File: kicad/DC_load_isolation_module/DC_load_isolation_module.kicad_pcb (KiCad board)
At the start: 2 copper layers, 110 x 60 mm, 200 parts, among them J1 Iso board connector, J12 Iso board connector, J2 USB_C_Receptacle_USB2.0_16P, Q1 MMBT5551L, Q10 AO3400A, Q11 AO3400A, Q12 MMBT5551L, Q13 AO3400A, Q14 MMBT5401, Q15 MMBT5551L, Q16 MMBT5551L, Q17 MMBT5401, Q18 MMBT5401, Q2 MMBT5401, Q26 MMBT5551L, Q27 MMBT5551L, Q28 MMBT5551L, Q29 MMBT5551L, Q3 MMBT5401, Q4 MMBT5551L, Q5 MMBT5401, Q6 MMBT5551L, Q7 MMBT5551L, Q8 MMBT5551L, Q9 MMBT5401, T1 UMEC_UT20A13S, T2 UMEC_UT20A13S, U1 LTV-817S, U2 MC34063AD, U3 LTV-817S, U4 CH340C, U5 74HC14D653

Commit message: Routing.
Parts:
- moved C53 4.29 mm to (136.2, 159.6), turned to 90 degrees
- moved C47 3.33 mm to (140.7, 159.6), turned to 90 degrees
- moved C49 1.41 mm to (139.2, 159.6), turned to 90 degrees
- moved R42 1.03 mm to (142.3, 159.6), turned to 90 degrees
- moved C51 0.78 mm to (137.7, 159.6), turned to 90 degrees
- moved D24 0.40 mm to (143.8, 184.3)
- moved R19 0.30 mm to (119.2, 156.3)
- moved Q12 0.28 mm to (116.4, 156.3)
- moved R49 0.14 mm to (130.5, 166.5)
- moved R40 0.10 mm to (134.2, 166.5)
- moved Q26 0.08 mm to (145.7, 171.9)
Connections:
- U5 pad 11: GND -> Earth
- U5 pad 13: GND -> Earth
- U5 pad 5: GND -> Earth
- U5 pad 9: GND -> Earth
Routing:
- net Earth: track 20.9 -> 71.0 mm, vias 19 -> 61
- net Net-(D19-K): track 0.00 -> 36.7 mm, vias 0 -> 1
- net 5V: track 53.1 -> 87.2 mm, vias 9 -> 14
- net Net-(JP1-B): track 0.00 -> 33.6 mm
- net 12V: track 0.00 -> 31.0 mm, vias 1 -> 8
- net Net-(Q26-C): track 0.00 -> 24.1 mm, vias 0 -> 1
- net GND: track 7.68 -> 30.9 mm, vias 8 -> 24
- net Net-(Q10-D): track 0.00 -> 19.8 mm
- net Net-(D4-K): track 0.00 -> 17.8 mm, vias 0 -> 1
- net ~{TF_GATE}: track 0.00 -> 17.5 mm, vias 0 -> 1
- net Net-(JP5-A): track 0.00 -> 16.1 mm, vias 1 -> 2
- net Net-(Q26-E): track 0.00 -> 15.0 mm, vias 0 -> 1
- net 11V: track 0.00 -> 14.5 mm, vias 0 -> 1
- net Net-(D3-K): track 0.00 -> 12.5 mm, vias 0 -> 2
- net 11V_SRF: track 0.00 -> 12.3 mm, vias 0 -> 1
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
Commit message: Connectors fixed.
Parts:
- added J3: Conn_01x03_Pin, Connector_PinHeader_2.54mm:PinHeader_1x03_P2.54mm_Vertical, F.Cu at (126.1, 189.8)
- J1: value Iso board connector -> PC referenced connector
- J12: value Iso board connector -> Load referenced connector; moved to F.Cu
- TP2, TP3: moved to F.Cu
- moved J1 102.8 mm to (157.7, 152.7)
- moved J12 45.1 mm to (52.3, 152.7), turned to 0 degrees
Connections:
- net 11V renamed /Isolated supply/11V
- net 11V_SRF renamed /Self resonating flyback/11V_SRF
- net 12V renamed 12V_PC
- net 5V renamed 5V_PC
- J1 pad 2: unconnected-(J1-Pin_2-Pad2) -> Earth
- J1 pad 3: unconnected-(J1-Pin_3-Pad3) -> 5V_PC_PC
- J1 pad 4: unconnected-(J1-Pin_4-Pad4) -> Earth
- J1 pad 8: GND -> unconnected-(J1-Pin_8-Pad8)
- J12 pad 2: 3V3 -> GND
- J12 pad 4: TX_3V3 -> GND
- J12 pad 5: GND -> TX_3V3
- J12 pad 6: 12V_EXT -> GND
- J12 pad 7: 5V_EXT -> 3V3
- J12 pad 8: Earth -> GND

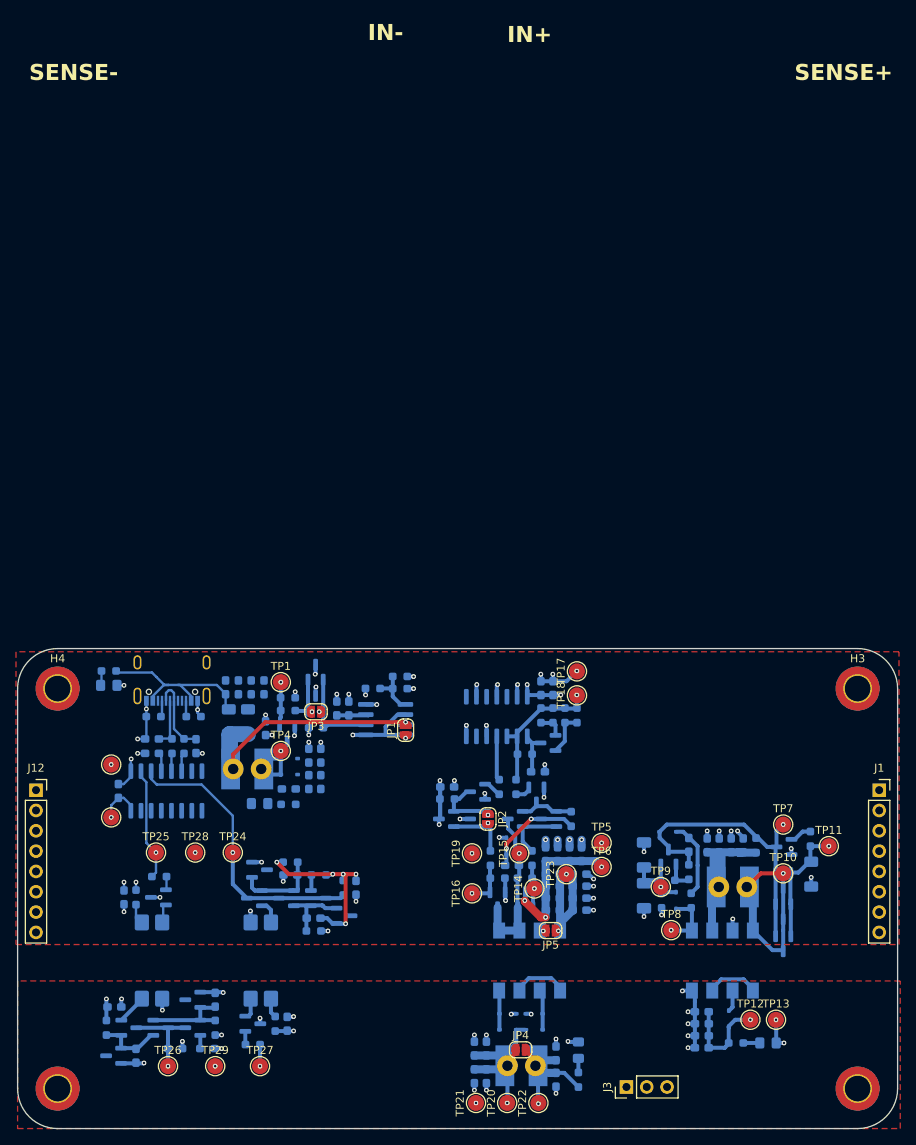
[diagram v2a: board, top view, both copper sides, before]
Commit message: Iso module almost done.
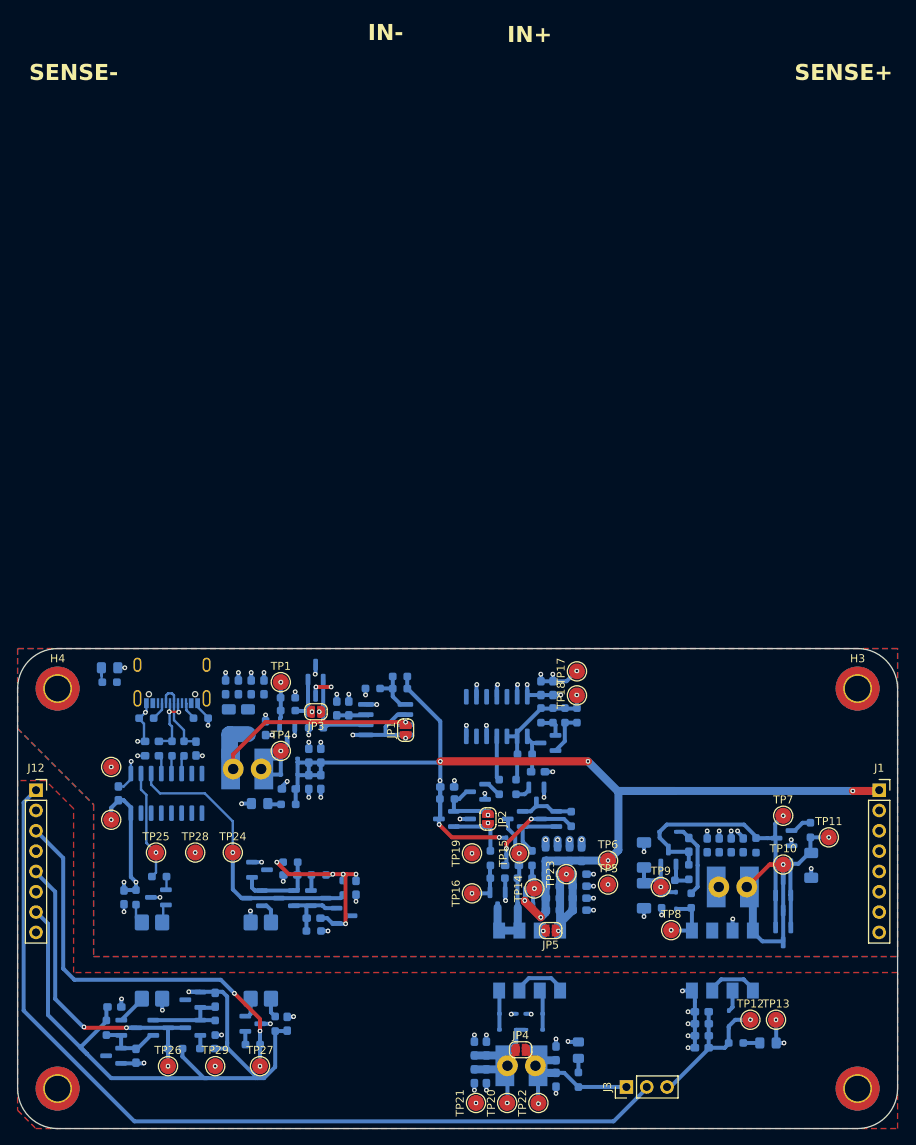
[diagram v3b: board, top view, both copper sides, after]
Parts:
- H1, H2: moved to F.Cu
- moved TP5 5.26 mm to (123.8, 164.5)
- moved D10 2.20 mm to (61.5, 137.4)
- moved R32 1.40 mm to (61.5, 139.2)
- moved TP6 1.13 mm to (123.8, 161.5)
- moved Q29 1.10 mm to (145.8, 158.7)
- moved Q26 1.10 mm to (145.7, 170.8)
- moved Q27 1.10 mm to (145.7, 166.8)
- moved Q28 1.10 mm to (145.7, 162.9)
- moved R47 1.10 mm to (149.2, 162.1)
- moved R48 1.10 mm to (149.1, 157.7)
- moved TP10 1.10 mm to (145.7, 162.0)
- moved TP11 1.10 mm to (151.4, 158.6)
- moved TP7 1.10 mm to (145.7, 155.9)
- moved R34 0.92 mm to (72.9, 143.7)
- moved R35 0.92 mm to (66.1, 143.7)
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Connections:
- J1 pad 3: 5V_PC_PC -> 5V_PC
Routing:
- net 12V_PC: track 31.0 -> 155.9 mm, vias 8 -> 9
- net VCC: track 0.00 -> 113.9 mm
- net 3V3: track 9.67 -> 84.8 mm, vias 5 -> 1
- net RX_3V3: track 2.60 -> 51.6 mm, vias 1 -> 3
- net TX_3V3: track 13.8 -> 43.7 mm, vias 1 -> 3
- net 5V_PC: track 87.2 -> 63.0 mm, vias 14 -> 15
- net Earth: track 71.0 -> 82.4 mm, vias 61 -> 69
- net /Self resonating flyback/11V_SRF: track 12.3 -> 19.7 mm
- net /Isolated supply/11V: track 14.5 -> 20.5 mm
- net Net-(C31-Pad1): track 6.60 -> 9.03 mm, vias 0 -> 2
- net Net-(D6-A): track 0.00 -> 1.57 mm
- net GND: track 30.9 -> 31.5 mm
- added copper zone on B.Cu, net 5V_PC

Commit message: Fixes
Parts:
- added D20: 1N5819WS, Diode_SMD:D_SOD-323, F.Cu at (89.0, 186.3)
- added D21: 1N5819WS, Diode_SMD:D_SOD-323, F.Cu at (89.0, 189.2)
- added R43: 100m, Resistor_SMD:R_1206_3216Metric_Pad1.30x1.75mm_HandSolder, F.Cu at (96.0, 180.6)
- added R44: 100m, Resistor_SMD:R_1206_3216Metric_Pad1.30x1.75mm_HandSolder, F.Cu at (96.0, 183.9)
- added R45: 100m, Resistor_SMD:R_1206_3216Metric_Pad1.30x1.75mm_HandSolder, F.Cu at (96.0, 187.2)
- added R46: 100, Resistor_SMD:R_0603_1608Metric_Pad0.98x0.95mm_HandSolder, F.Cu at (101.2, 180.2)
- added R50: 100, Resistor_SMD:R_0603_1608Metric_Pad0.98x0.95mm_HandSolder, F.Cu at (101.2, 182.7)
- added R51: 100, Resistor_SMD:R_0603_1608Metric_Pad0.98x0.95mm_HandSolder, F.Cu at (101.2, 185.2)
- D12, D14: value BAV99 -> 1N5819WS; footprint Package_TO_SOT_SMD:SOT-23 -> Diode_SMD:D_SOD-323; moved to F.Cu
- moved D12 21.1 mm to (89.0, 180.4)
- moved D14 18.0 mm to (89.0, 183.3), turned to 0 degrees
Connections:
- C27 pad 2: Net-(Q7-B) -> Net-(D21-K)
- C29 pad 1: Net-(D13-A) -> Net-(D12-A)
- D1 pad 1: Net-(Q7-B) -> Net-(D21-K)
- D12 pad 1: Net-(Q7-B) -> /Boost/RX
- D12 pad 2: Net-(D11-A) -> Net-(D12-A)
- D13 pad 2: Net-(D13-A) -> Net-(D12-A)
- D14 pad 2: Net-(D13-A) -> /Boost/RX
- Q18 pad 1: Net-(D13-A) -> Net-(D12-A)
- Q26 pad 1: Net-(D19-K) -> Net-(Q26-B)
- Q27 pad 1: Net-(D19-K) -> Net-(Q27-B)
- Q27 pad 2: Net-(Q26-E) -> Net-(Q27-E)
- Q28 pad 1: Net-(D19-K) -> Net-(Q28-B)
- Q28 pad 2: Net-(Q26-E) -> Net-(Q28-E)
- Q7 pad 1: Net-(Q7-B) -> Net-(D21-K)
- R25 pad 1: Net-(Q7-B) -> Net-(D21-K)
- R28 pad 1: Net-(D13-A) -> Net-(D12-A)
- R47 pad 2: Net-(Q26-E) -> Net-(R43-Pad1)
- R48 pad 1: Net-(Q26-E) -> Net-(R43-Pad1)
- TP11 pad 1: Net-(Q26-E) -> Net-(R43-Pad1)
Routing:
- net Net-(D13-A): track 8.71 -> 0.00 mm
- net Net-(D12-A): track 0.00 -> 8.71 mm
- net Net-(Q7-B): track 7.79 -> 0.00 mm
- net Net-(D21-K): track 0.00 -> 7.79 mm

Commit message: kfsald
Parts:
- removed D14, D20, D21: 1N5819WS, Diode_SMD:D_SOD-323
- added D23: BAV99, Package_TO_SOT_SMD:SOT-23, B.Cu at (83.7, 166.2)
- D12: value 1N5819WS -> BAV99; footprint Diode_SMD:D_SOD-323 -> Package_TO_SOT_SMD:SOT-23; moved to B.Cu
- R43, R44, R45, R46, R50, R51: moved to B.Cu
- moved R43 59.6 mm to (153.9, 166.4), turned to -90 degrees
- moved R45 57.9 mm to (150.1, 166.4), turned to -90 degrees
- moved R51 53.9 mm to (152.0, 167.2), turned to 90 degrees
- moved R44 53.2 mm to (146.3, 166.4), turned to -90 degrees
- moved R46 48.8 mm to (148.2, 167.2), turned to 90 degrees
- moved R50 45.9 mm to (144.4, 167.2), turned to 90 degrees
- moved D12 21.1 mm to (68.0, 182.4)
- moved Q28 10.6 mm to (152.7, 170.8)
- moved TP7 9.24 mm to (144.1, 165.0)
- moved Q27 5.32 mm to (149.2, 170.8)
- moved TP11 3.75 mm to (148.6, 161.1)
- moved TP10 1.60 mm to (144.1, 162.0)
- moved R48 1.22 mm to (148.6, 158.8)
- moved R47 0.51 mm to (149.1, 162.6), turned to 0 degrees
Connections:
- C27 pad 2: Net-(D21-K) -> Net-(Q7-B)
- C29 pad 1: Net-(D12-A) -> Net-(D13-A)
- D1 pad 1: Net-(D21-K) -> Net-(Q7-B)
- D12 pad 1: /Boost/RX -> Net-(Q7-B)
- D12 pad 2: Net-(D12-A) -> Net-(D11-A)
- D13 pad 2: Net-(D12-A) -> Net-(D13-A)
- Q18 pad 1: Net-(D12-A) -> Net-(D13-A)
- Q7 pad 1: Net-(D21-K) -> Net-(Q7-B)
- R25 pad 1: Net-(D21-K) -> Net-(Q7-B)
- R28 pad 1: Net-(D12-A) -> Net-(D13-A)
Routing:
- net Net-(R43-Pad1): track 0.00 -> 13.4 mm, vias 0 -> 1
- net Net-(Q26-E): track 15.0 -> 1.78 mm, vias 1 -> 0
- net Net-(Q26-C): track 24.5 -> 12.4 mm
- net Net-(D13-A): track 0.00 -> 8.71 mm
- net Net-(D12-A): track 8.71 -> 0.00 mm
- net Net-(Q7-B): track 0.00 -> 7.79 mm
- net Net-(D21-K): track 7.79 -> 0.00 mm
- net Net-(Q27-E): track 0.00 -> 1.88 mm
- net Net-(D19-K): track 36.4 -> 38.3 mm
- net Net-(Q28-B): track 0.00 -> 1.81 mm
- net Net-(Q27-B): track 0.00 -> 1.78 mm
- net Net-(Q28-E): track 0.00 -> 1.78 mm
- net Net-(Q26-B): track 0.00 -> 1.71 mm
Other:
- board text added: "11V"
- board text added: "12V"
- board text added: "5V"
- board text added: "AUX"
- board text added: "BASE"
- board text added: "COLLECTOR"
- board text added: "CP"
- board text added: "DRAIN"
- board text added: "GATE"
- board text added: "GND"
- board text added: "HB"
- board text added: "HG"
- board text added: "LG"
- board text added: "MP"
- board text added: "OUT"
- board text added: "RX"
- board text added: "SHUNT"
- board text added: "SRF"
- board text added: "TF_GATE"
- board text added: "TX"
- board text added: "ZNR"

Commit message: pre prod
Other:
- board text removed: "IN+"
- board text removed: "IN-"
- board text removed: "SENSE+"
- board text removed: "SENSE-"
